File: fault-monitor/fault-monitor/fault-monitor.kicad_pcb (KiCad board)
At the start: 2 copper layers, 73 x 75.5 mm, 21 parts, among them J1 Conn_01x03, J2 Conn_01x06, J3 Conn_01x02, J4 Conn_01x02, J5 Conn_01x02, J6 Conn_01x02, J7 Conn_01x06, U1 ESP32-DevKitC

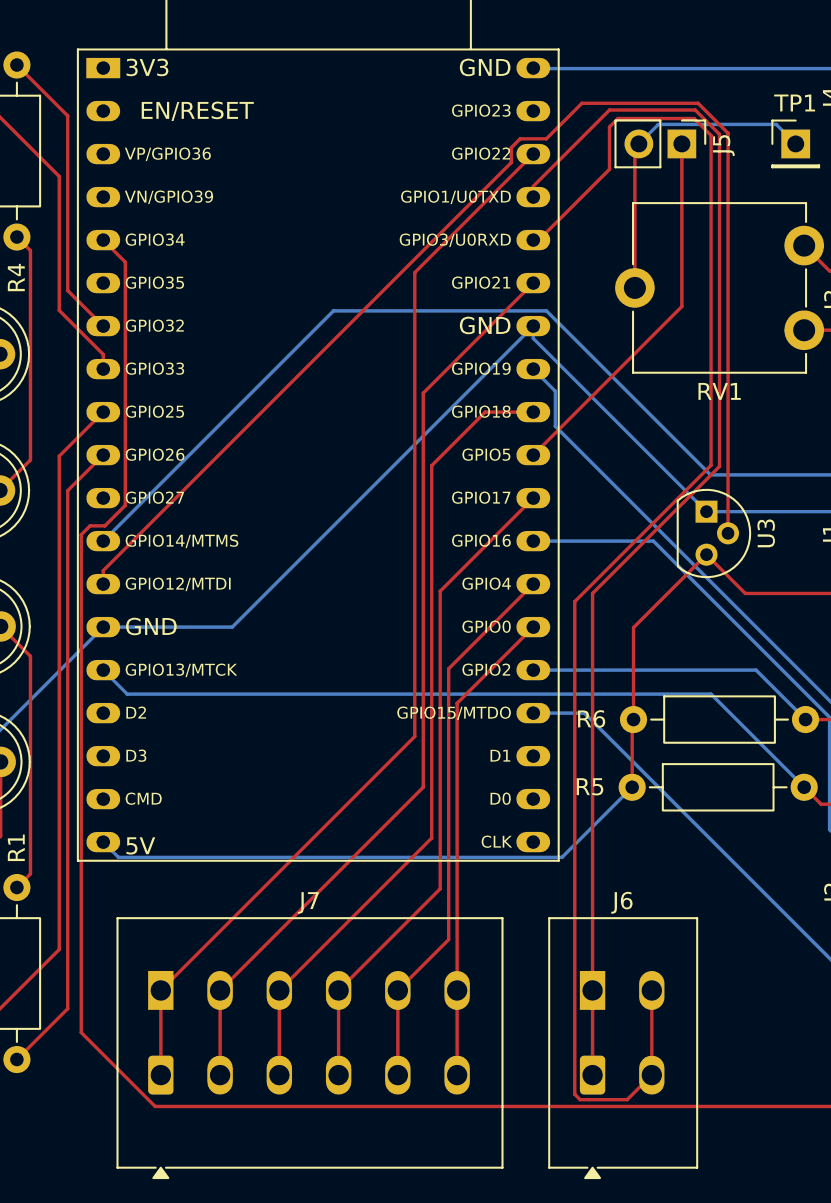
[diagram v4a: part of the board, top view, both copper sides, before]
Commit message: reroute to make tx and tx lines shorter and straighter
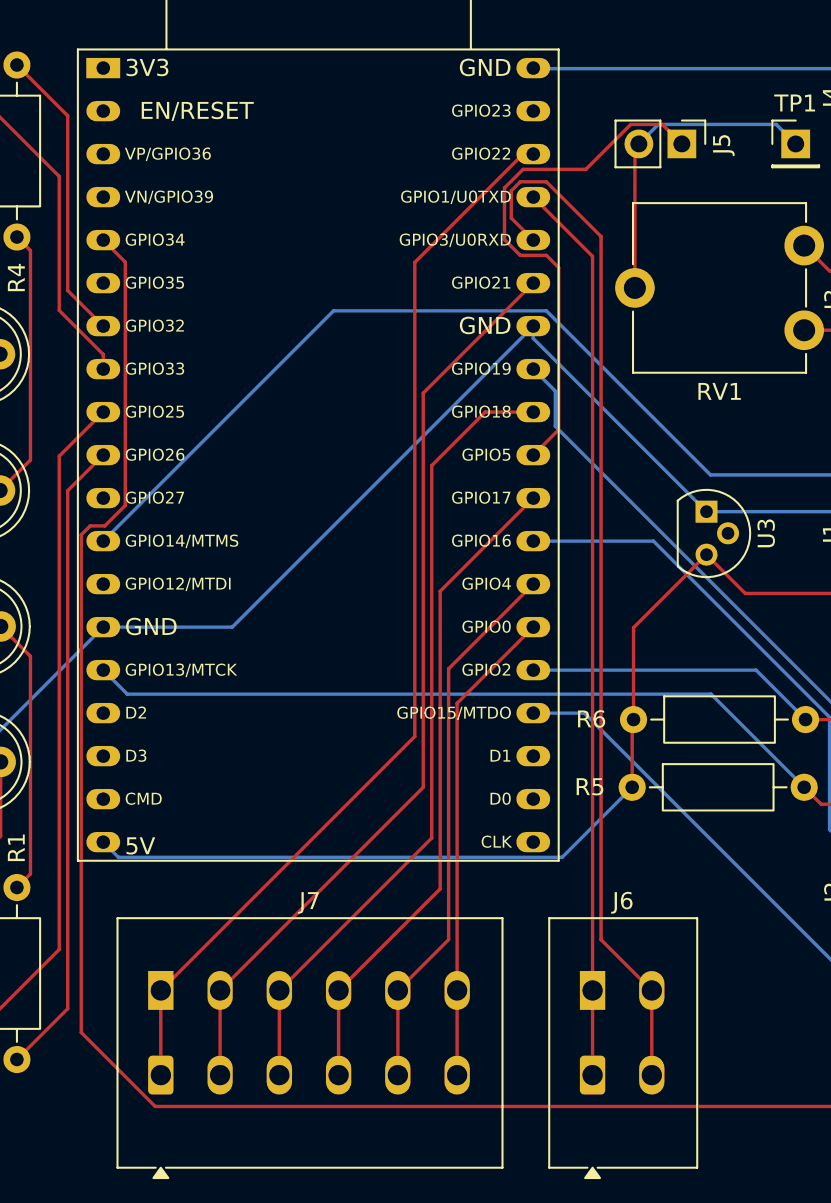
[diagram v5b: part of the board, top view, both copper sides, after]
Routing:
- net Net-(U1-IO12): track 74.0 -> 0.00 mm
- net Net-(J6-Pin_2): track 85.6 -> 61.1 mm
- net Net-(J6-Pin_1): track 72.8 -> 53.3 mm
- net Net-(J5-Pin_1): track 22.0 -> 31.1 mm
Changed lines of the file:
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@@
 	)
 	(segment
-		(start 96.275 53)
-		(end 96.275 62.605)
-		(width 0.2)
-		(layer "F.Cu")
-		(net 17)
-	)
-	(segment
-		(start 96.275 62.605)
-		(end 87.5 71.38)
-		(width 0.2)
-		(layer "F.Cu")
-		(net 17)
-	)
-	(segment
-		(start 98 52.5)
-		(end 98 71.9809)
-		(width 0.2)
-		(layer "F.Cu")
-		(net 18)
+		(start 90.60624 54.501)
+		(end 93.25824 51.849)
+		(width 0.2)
+		(layer "F.Cu")
+		(net 17)
+	)
+	(segment
+		(start 85.798 58.652206)
+		(end 85.798 55.600694)
+		(width 0.2)
+		(layer "F.Cu")
+		(net 17)
+	)
+	(segment
+		(start 86.897694 54.501)
+		(end 90.60624 54.501)
+		(width 0.2)
+		(layer "F.Cu")
+		(net 17)
+	)
+	(segment
+		(start 88.273206 59.581)
+		(end 86.726794 59.581)
+		(width 0.2)
+		(layer "F.Cu")
+		(net 17)
+	)
+	(segment
+		(start 93.25824 51.849)
+		(end 95.124 51.849)
+		(width 0.2)
+		(layer "F.Cu")
+		(net 17)
+	)
+	(segment
+		(start 89 69.88)
+		(end 89 60.307794)
+		(width 0.2)
+		(layer "F.Cu")
+		(net 17)
+	)
+	(segment
+		(start 89 60.307794)
+		(end 88.273206 59.581)
+		(width 0.2)
+		(layer "F.Cu")
+		(net 17)
+	)
+	(segment
+		(start 95.124 51.849)
+		(end 96.275 53)
+		(width 0.2)
+		(layer "F.Cu")
+		(net 17)
+	)
+	(segment
+		(start 85.798 55.600694)
+		(end 86.897694 54.501)
+		(width 0.2)
+		(layer "F.Cu")
+		(net 17)
+	)
+	(segment
+		(start 87.5 71.38)
+		(end 89 69.88)
+		(width 0.2)
+		(layer "F.Cu")
+		(net 17)
+	)
+	(segment
+		(start 86.726794 59.581)
+		(end 85.798 58.652206)
+		(width 0.2)
+		(layer "F.Cu")
+		(net 17)
 	)
 	(segment
@@
 	)
 	(segment
-		(start 97 51.5)
-		(end 98 52.5)
-		(width 0.2)
-		(layer "F.Cu")
-		(net 18)
-	)
-	(segment
-		(start 93.049 109.451)
-		(end 94.5 108)
+		(start 86.199 55.766794)
+		(end 86.726794 55.239)
+		(width 0.2)
+		(layer "F.Cu")
+		(net 18)
+	)
+	(segment
+		(start 91.5 100)
+		(end 94.5 103)
+		(width 0.2)
+		(layer "F.Cu")
+		(net 18)
+	)
+	(segment
+		(start 91.5 58.465794)
+		(end 91.5 100)
+		(width 0.2)
+		(layer "F.Cu")
+		(net 18)
+	)
+	(segment
+		(start 86.199 57.379)
+		(end 86.199 55.766794)
+		(width 0.2)
+		(layer "F.Cu")
+		(net 18)
+	)
+	(segment
+		(start 88.273206 55.239)
+		(end 91.5 58.465794)
 		(width 0.2)
 		(layer "F.Cu")
@@
 	(segment
 		(start 87.5 58.68)
-		(end 87.82 58.68)
-		(width 0.2)
-		(layer "F.Cu")
-		(net 18)
-	)
-	(segment
-		(start 87.82 58.68)
-		(end 92 54.5)
-		(width 0.2)
-		(layer "F.Cu")
-		(net 18)
-	)
-	(segment
-		(start 92 54.5)
-		(end 92 52)
-		(width 0.2)
-		(layer "F.Cu")
-		(net 18)
-	)
-	(segment
-		(start 92.5 51.5)
-		(end 97 51.5)
-		(width 0.2)
-		(layer "F.Cu")
-		(net 18)
-	)
-	(segment
-		(start 89.949 109.13516)
-		(end 90.26484 109.451)
-		(width 0.2)
-		(layer "F.Cu")
-		(net 18)
-	)
-	(segment
-		(start 90.26484 109.451)
-		(end 93.049 109.451)
-		(width 0.2)
-		(layer "F.Cu")
-		(net 18)
-	)
-	(segment
-		(start 92 52)
-		(end 92.5 51.5)
-		(width 0.2)
-		(layer "F.Cu")
-		(net 18)
-	)
-	(segment
-		(start 89.949 80.0319)
-		(end 89.949 109.13516)
-		(width 0.2)
-		(layer "F.Cu")
-		(net 18)
-	)
-	(segment
-		(start 98 71.9809)
-		(end 89.949 80.0319)
-		(width 0.2)
-		(layer "F.Cu")
-		(net 18)
-	)
-	(segment
-		(start 91 79.548)
-		(end 91 103)
-		(width 0.2)
-		(layer "F.Cu")
-		(net 19)
-	)
-	(segment
-		(start 87.5 55.5)
-		(end 92 51)
-		(width 0.2)
-		(layer "F.Cu")
-		(net 19)
-	)
-	(segment
-		(start 92 51)
-		(end 97.0671 51)
-		(width 0.2)
-		(layer "F.Cu")
-		(net 19)
-	)
-	(segment
-		(start 98.5 52.4329)
-		(end 98.5 72.048)
-		(width 0.2)
-		(layer "F.Cu")
-		(net 19)
-	)
-	(segment
-		(start 98.5 72.048)
-		(end 91 79.548)
-		(width 0.2)
-		(layer "F.Cu")
-		(net 19)
-	)
-	(segment
-		(start 97.0671 51)
-		(end 98.5 52.4329)
+		(end 86.199 57.379)
+		(width 0.2)
+		(layer "F.Cu")
+		(net 18)
+	)
+	(segment
+		(start 86.726794 55.239)
+		(end 88.273206 55.239)
+		(width 0.2)
+		(layer "F.Cu")
+		(net 18)
+	)
+	(segment
+		(start 87.5 56.14)
+		(end 91 59.64)
 		(width 0.2)
 		(layer "F.Cu")
@@
 	)
 	(segment
-		(start 87.5 56.14)
-		(end 87.5 55.5)
+		(start 91 59.64)
+		(end 91 103)
 		(width 0.2)
 		(layer "F.Cu")
@@
 	)
 	(segment
-		(start 80.5 88)
-		(end 80.5 60.6)
-		(width 0.2)
-		(layer "F.Cu")
-		(net 20)
-	)
-	(segment
-		(start 65.5 103)
-		(end 80.5 88)
+		(start 86.9 53.6)
+		(end 80.5 60)
 		(width 0.2)
 		(layer "F.Cu")
@@
 	)
 	(segment
-		(start 80.5 60.6)
-		(end 87.5 53.6)
+		(start 80.5 88)
+		(end 65.5 103)
+		(width 0.2)
+		(layer "F.Cu")
+		(net 20)
+	)
+	(segment
+		(start 87.5 53.6)
+		(end 86.9 53.6)
+		(width 0.2)
+		(layer "F.Cu")
+		(net 20)
+	)
+	(segment
+		(start 80.5 60)
+		(end 80.5 88)
 		(width 0.2)
 		(layer "F.Cu")
@@
 		(net 29)
 	)
-	(segment
-		(start 86.199 54.101)
-		(end 86.199 53.226794)
-		(width 0.2)
-		(layer "F.Cu")
-		(net 43)
-	)
-	(segment
-		(start 62.1 79)
-		(end 62.1 78.2)
-		(width 0.2)
-		(layer "F.Cu")
-		(net 43)
-	)
-	(segment
-		(start 97.2332 50.599)
-		(end 99 52.3658)
-		(width 0.2)
-		(layer "F.Cu")
-		(net 43)
-	)
-	(segment
-		(start 86.199 53.226794)
-		(end 86.726794 52.699)
-		(width 0.2)
-		(layer "F.Cu")
-		(net 43)
-	)
-	(segment
-		(start 86.726794 52.699)
-		(end 88.273206 52.699)
-		(width 0.2)
-		(layer "F.Cu")
-		(net 43)
-	)
-	(segment
-		(start 90.373206 50.599)
-		(end 97.2332 50.599)
-		(width 0.2)
-		(layer "F.Cu")
-		(net 43)
-	)
-	(segment
-		(start 88.273206 52.699)
-		(end 90.373206 50.599)
-		(width 0.2)
-		(layer "F.Cu")
-		(net 43)
-	)
-	(segment
-		(start 62.1 78.2)
-		(end 86.199 54.101)
-		(width 0.2)
-		(layer "F.Cu")
-		(net 43)
-	)
-	(segment
-		(start 99 52.3658)
-		(end 99 76)
-		(width 0.2)
-		(layer "F.Cu")
-		(net 43)
-	)
 	(embedded_fonts no)

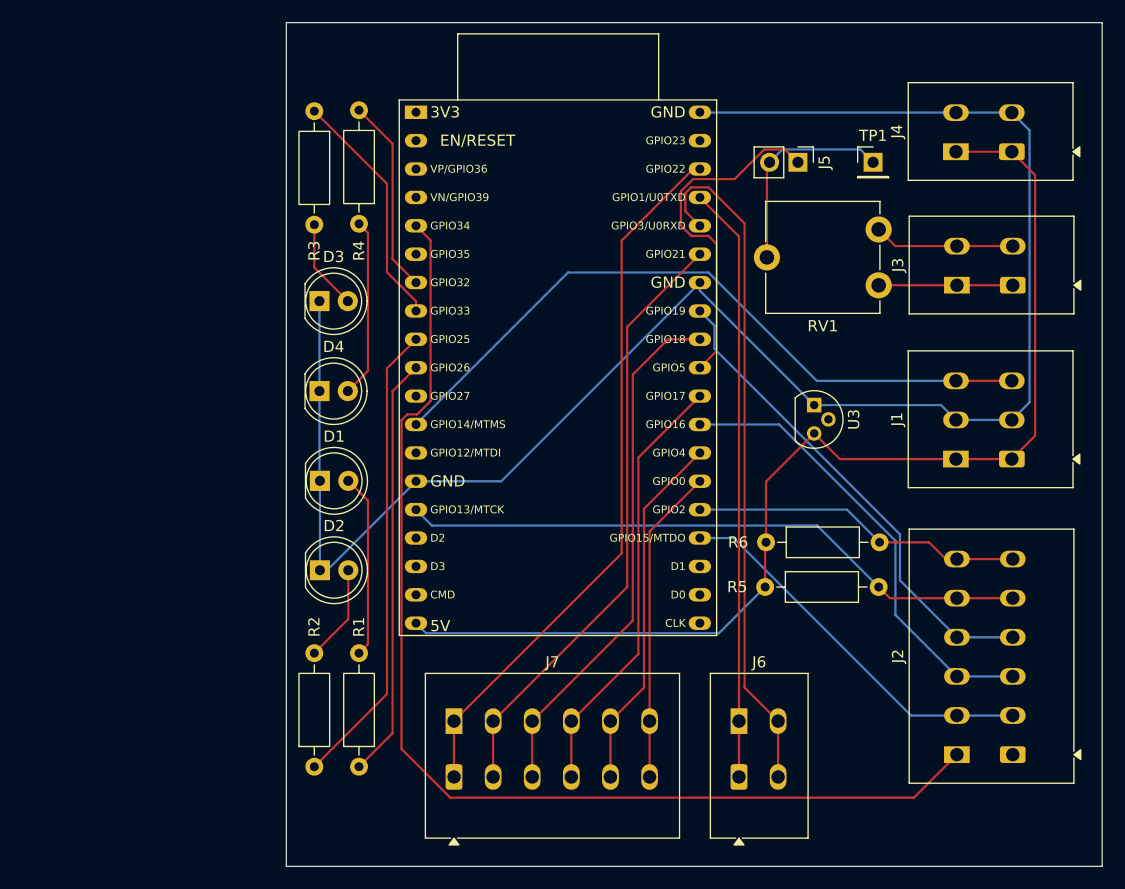
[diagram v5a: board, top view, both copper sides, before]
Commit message: add wago 3d models
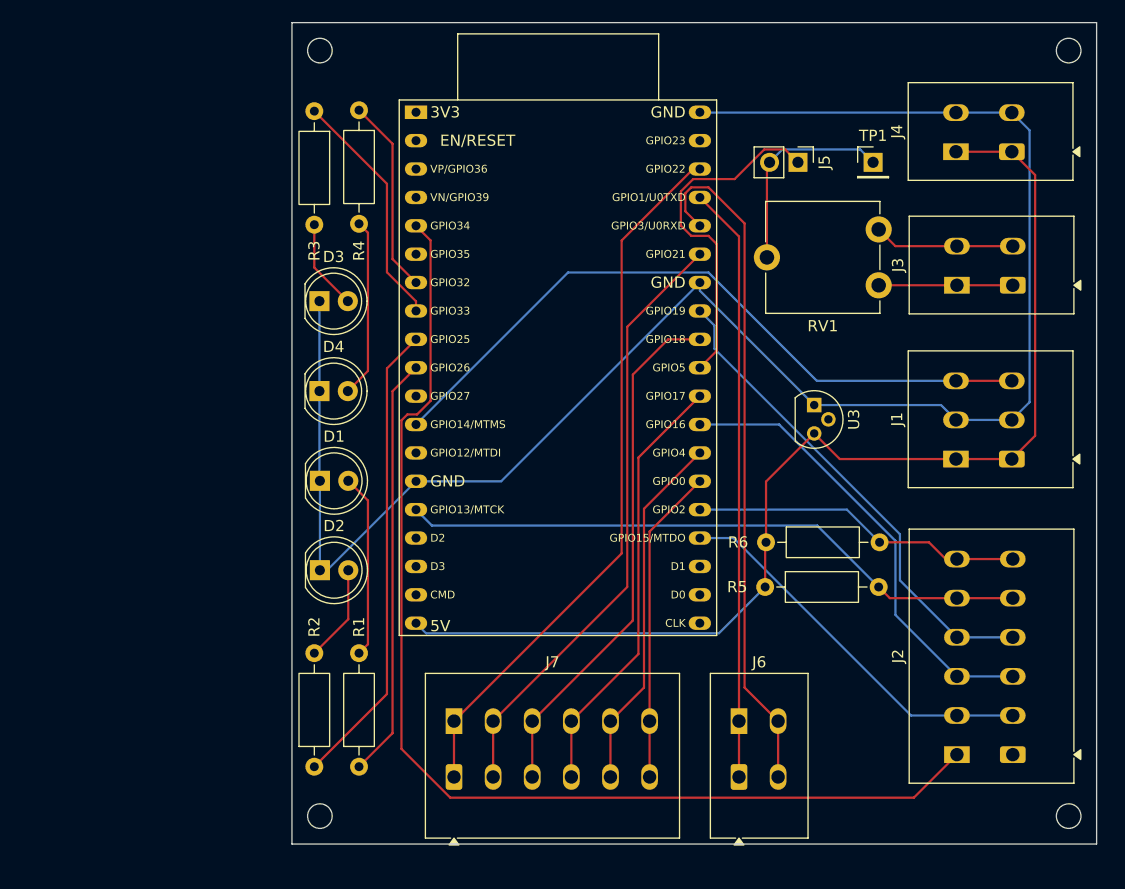
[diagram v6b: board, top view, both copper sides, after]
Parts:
- added REF**: MountingHole_2.2mm_M2, MountingHole:MountingHole_2.2mm_M2, F.Cu at (120.5, 43.0)
- added REF**: MountingHole_2.2mm_M2, MountingHole:MountingHole_2.2mm_M2, F.Cu at (53.5, 111.5)
- added REF**: MountingHole_2.2mm_M2, MountingHole:MountingHole_2.2mm_M2, F.Cu at (53.5, 43.0)
- added REF**: MountingHole_2.2mm_M2, MountingHole:MountingHole_2.2mm_M2, F.Cu at (120.5, 111.5)
- J1: footprint TerminalBlock_WAGO:TerminalBlock_WAGO_2601-1103_1x03_P3.50mm_Horizontal -> TerminalBlock_WAGO_3D:TerminalBlock_WAGO_2601-1103_1x03_P3.50mm_Horizontal-3D
- J2, J7: footprint TerminalBlock_WAGO:TerminalBlock_WAGO_2601-1106_1x06_P3.50mm_Horizontal -> TerminalBlock_WAGO_3D:TerminalBlock_WAGO_2601-1106_1x06_P3.50mm_Horizontal-3D
- J3, J4, J6: footprint TerminalBlock_WAGO:TerminalBlock_WAGO_2601-1102_1x02_P3.50mm_Horizontal -> TerminalBlock_WAGO_3D:TerminalBlock_WAGO_2601-1102_1x02_P3.50mm_Horizontal-3D
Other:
- board size 73 x 75.5 mm -> 72 x 73.5 mm

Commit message: oops forgot to route one thing
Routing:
- net Net-(U1-IO12): track 0.00 -> 50.4 mm
- net GND: track 158.9 -> 160.8 mm
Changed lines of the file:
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@@
+	)
+	(segment
+		(start 97.73 74.72)
+		(end 109.08344 74.72)
+		(width 0.2)
+		(layer "F.Cu")
+		(net 1)
+	)
+	(segment
+		(start 109.08344 74.72)
+		(end 110.415 76.05156)
+		(width 0.2)
+		(layer "F.Cu")
+		(net 1)
 	)
 	(segment
@@
 	)
 	(segment
-		(start 109.08344 74.72)
-		(end 97.73 74.72)
-		(width 0.2)
-		(layer "B.Cu")
-		(net 1)
-	)
-	(segment
 		(start 87.5 63.76)
 		(end 87.5 64.49)
@@
 	)
 	(segment
-		(start 115.415 72.55156)
+		(start 110.415 72.55156)
+		(end 115.415 72.55156)
+		(width 0.2)
+		(layer "B.Cu")
+		(net 7)
+	)
+	(segment
+		(start 62.1 76.46)
+		(end 76.102 62.458)
+		(width 0.2)
+		(layer "B.Cu")
+		(net 7)
+	)
+	(segment
+		(start 102.05156 72.55156)
 		(end 110.415 72.55156)
 		(width 0.2)
-		(layer "F.Cu")
+		(layer "B.Cu")
 		(net 7)
 	)
 	(segment
-		(start 88.273206 62.859)
-		(end 75.701 62.859)
+		(start 91.958 62.458)
+		(end 102.05156 72.55156)
 		(width 0.2)
 		(layer "B.Cu")
@@
 	)
 	(segment
-		(start 75.701 62.859)
-		(end 62.1 76.46)
-		(width 0.2)
-		(layer "B.Cu")
-		(net 7)
-	)
-	(segment
-		(start 110.415 72.55156)
-		(end 97.965766 72.55156)
-		(width 0.2)
-		(layer "B.Cu")
-		(net 7)
-	)
-	(segment
-		(start 97.965766 72.55156)
-		(end 88.273206 62.859)
+		(start 76.102 62.458)
+		(end 91.958 62.458)
 		(width 0.2)
 		(layer "B.Cu")
@@
 		(net 29)
 	)
+	(segment
+		(start 88.273206 62.859)
+		(end 78.241 62.859)
+		(width 0.2)
+		(layer "B.Cu")
+		(net 43)
+	)
+	(segment
+		(start 99 76)
+		(end 99 73.585794)
+		(width 0.2)
+		(layer "B.Cu")
+		(net 43)
+	)
+	(segment
+		(start 99 73.585794)
+		(end 88.273206 62.859)
+		(width 0.2)
+		(layer "B.Cu")
+		(net 43)
+	)
+	(segment
+		(start 78.241 62.859)
+		(end 62.1 79)
+		(width 0.2)
+		(layer "B.Cu")
+		(net 43)
+	)
 	(embedded_fonts no)

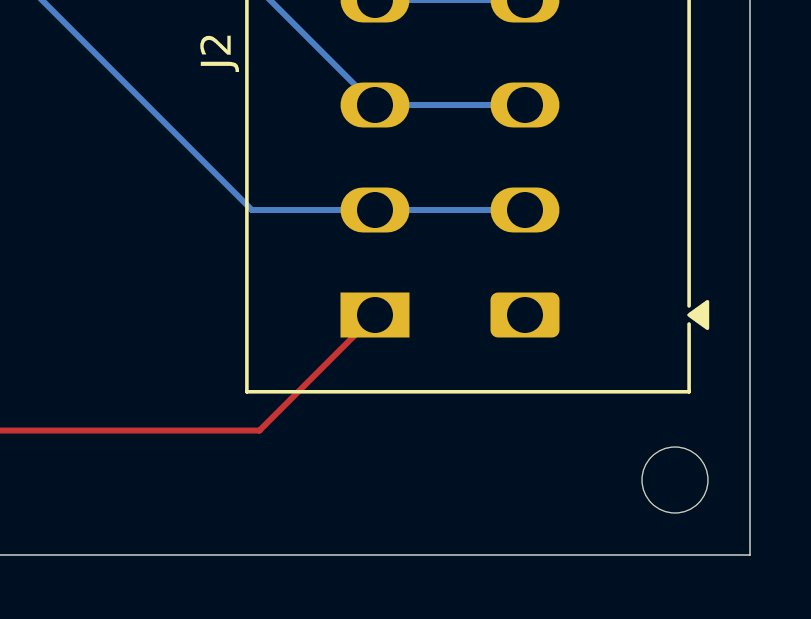
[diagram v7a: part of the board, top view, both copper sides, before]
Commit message: missed another trace
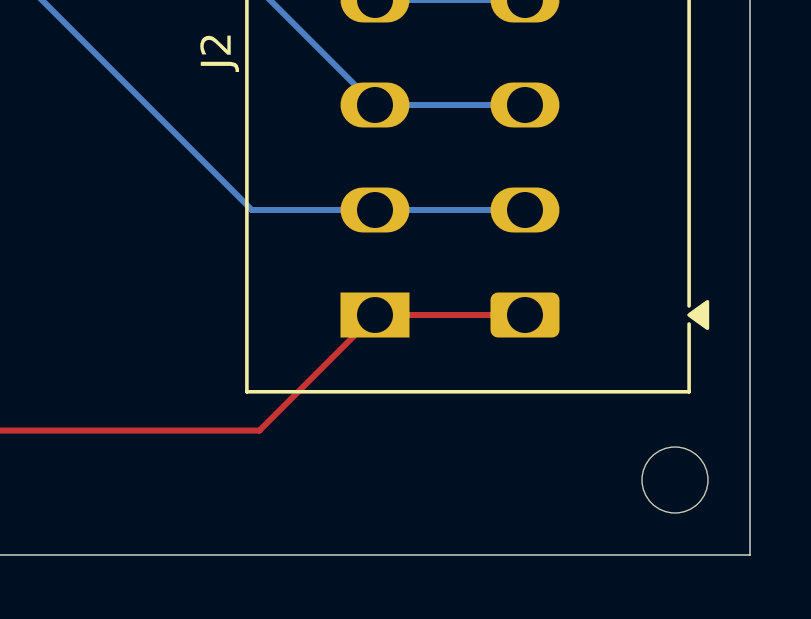
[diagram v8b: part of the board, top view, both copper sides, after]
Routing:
- net /STOPALL: track 102.0 -> 107.0 mm
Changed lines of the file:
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@@
+	)
+	(segment
+		(start 110.5 106)
+		(end 115.5 106)
+		(width 0.2)
+		(layer "F.Cu")
+		(net 12)
 	)
 	(segment
